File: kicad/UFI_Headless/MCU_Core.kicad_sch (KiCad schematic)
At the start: 76 parts, among them J12 FRONT, J4 SWD, J5 DBG_UART, SW1 RESET, SW2 BOOT, SW3 BTN_A, SW4 BTN_B, U11 APS6404L-3SQR-SN, U15 CSNP32GCR01-AOW, U5 STM32H723ZGT6, Y1 25MHz CL=12pF

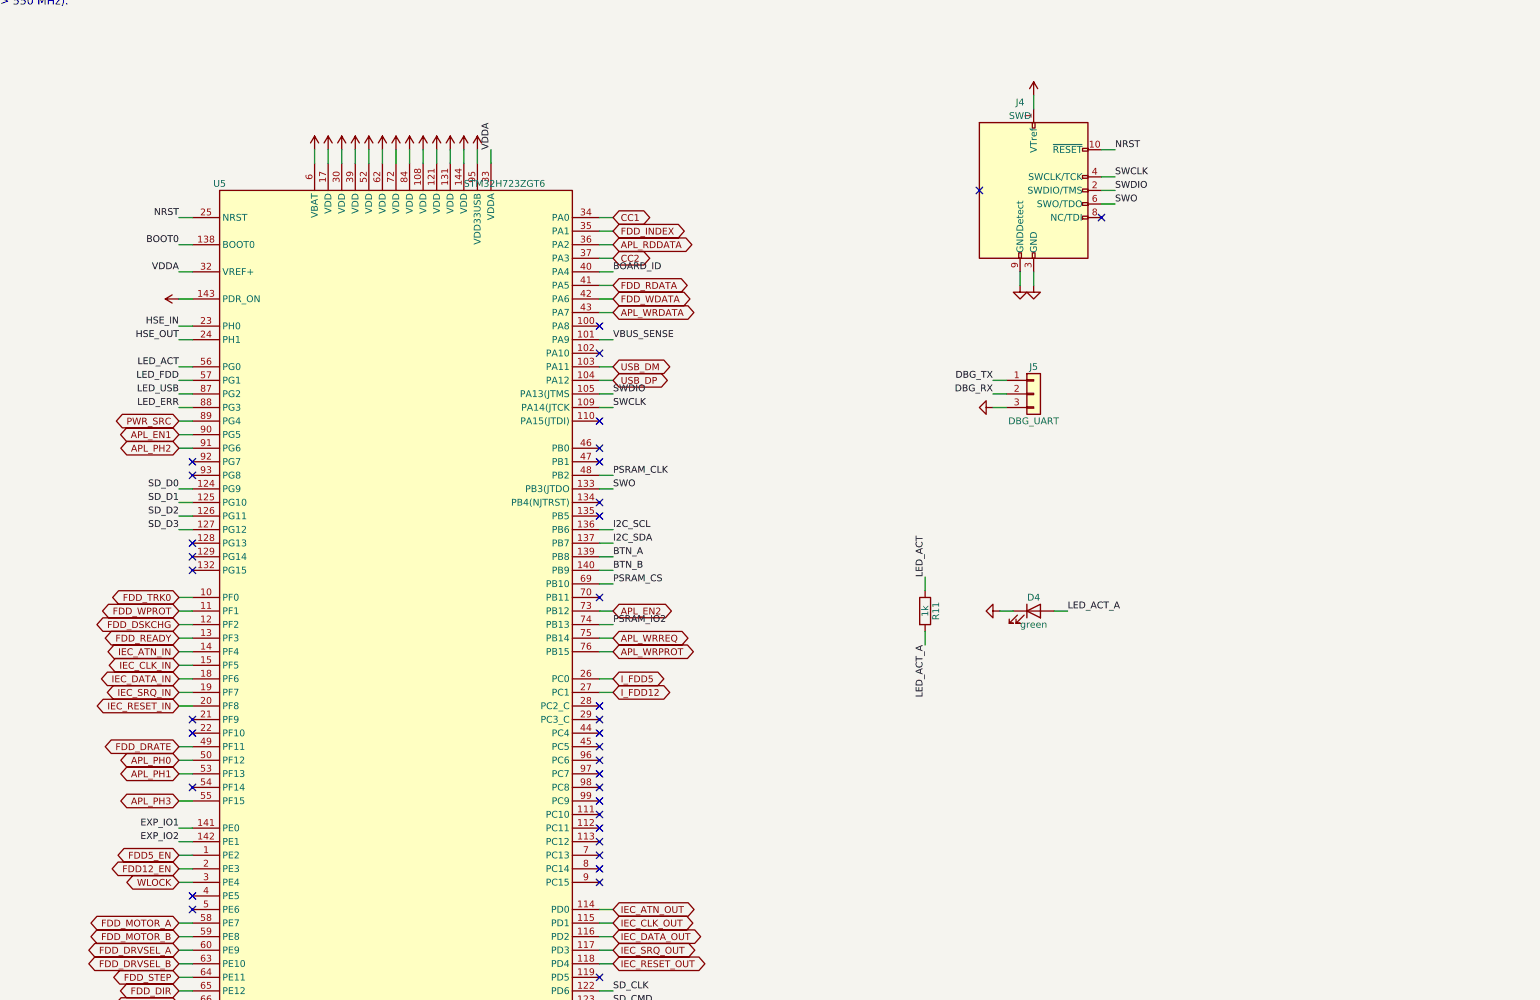
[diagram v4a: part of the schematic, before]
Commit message: KiCad v0.7 rework, schematic stage A4 with the matching firmware pin map: electronic self-test loopback, index simulation on its own timer pin, PSU-guard header, LA header - owner's constraint of 2026-10-24: the board sits in a closed enclosure, only LAN and USB stay reachable, nothing is pluggable after assembly, so no jumpers or slide switches for operation. Flux_Interface: J11 WRITE_LOCK pin header replaced by solder jumper JP4 (+3V3 to WLOCK, R33 100k pull-down and the U14 LVC1G32 hardware gate unchanged); INDEX_SIM is a global net from PE5 (TIM15_CH1, verified against the ST pin database via the embassy stm32h723zg tables) through the until now unused open-collector buffer U7F (pin 13 was tied to +5V) onto FD_INDEX, wired-OR like the J19 sync sensor, so the self-test index loop needs no wire; new loopback block U22 TS5A3166DBVR (SOT-23-5, pins 1 NO = FD_RDATA, 2 COM = FD_WDATA, 3 GND, 4 IN = LOOP_EN, 5 V+ = +5V; TI datasheet: V+ 1.65-5.5 V, VIH 2.4 V at 5 V, control input 0-5.5 V), C58 100n, R106 100k pull-down on LOOP_EN (open during reset), Q5 2N7002 pulls FD_TRK0 low with LOOP_EN; note text updated. IEC_Bus: the spare inverter U10F (input was GND, output no-connect) reads FD_WGATE back as WGATE_SENSE. MCU_Core: U5 PE5 INDEX_SIM, PG14 LOOP_EN, PG15 WGATE_SENSE, PG7 GUARD_OFF, PG8 GUARD_ERR5, PG13 GUARD_ERR12 (six no-connect flags removed); J20 GUARD 1x4 (1 GND, 2 OFF, 3 ERR5, 4 ERR12 with R107/R108 10k pull-ups) for the C64 PSU Guard board's J3; J21 LA 2x10 logic-analyser header on the 3.3 V side (1 RDATA, 3 WDATA, 5 INDEX, 7 WGATE, 9 STEP, 11 DIR, 13 SIDE, 15 DRVSEL_A, 17 MOTOR_A, 19 TRK0, 2 WPROT, 4 DSKCHG, 6 READY, 8 DENSITY, 10 INDEX_SIM, 12 LOOP_EN, 14 WGATE_SENSE, 16/18/20 GND); lib symbols TS5A3166DBVR, 2N7002, SolderJumper_2_Open, Conn_01x04, Conn_02x10_Odd_Even added to the sheets. ERC over the whole project 0 errors / 0 warnings. Firmware (same commit, as agreed): board.h/board_headless.c pin table PIN_INDEX_SIM PE5 (INDEX_SIM_AF = AF4), PIN_LOOP_EN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
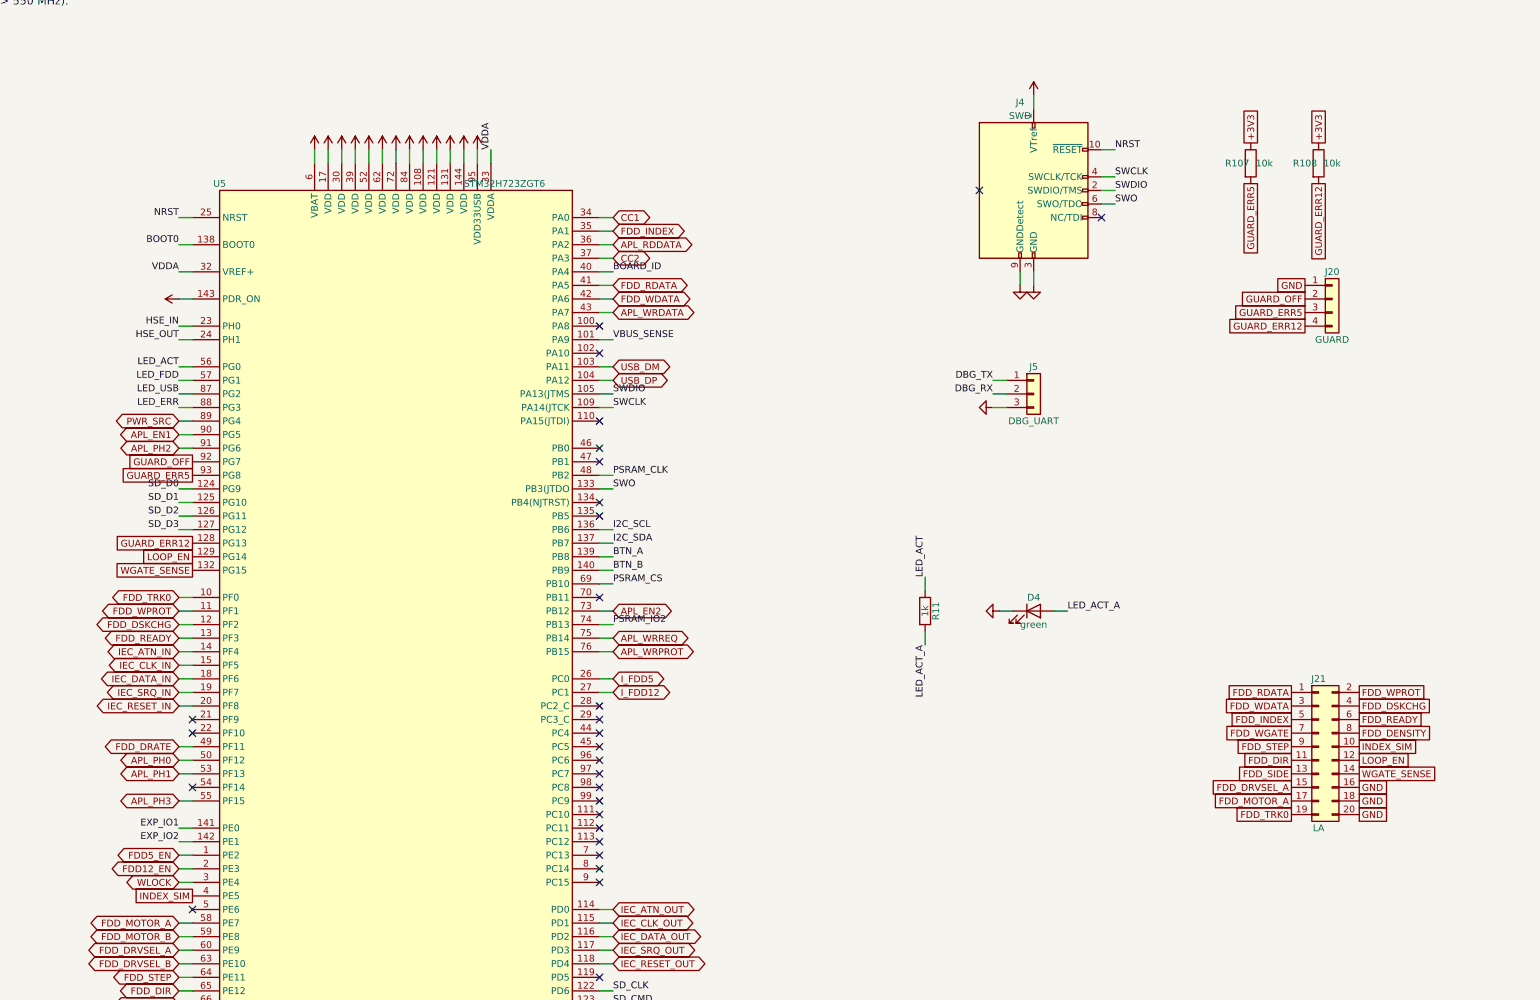
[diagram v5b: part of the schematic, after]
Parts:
- added J20: GUARD, Connector_PinHeader_2.54mm:PinHeader_1x04_P2.54mm_Vertical, symbol Connector_Generic:Conn_01x04
- added J21: LA, Connector_PinHeader_2.54mm:PinHeader_2x10_P2.54mm_Vertical, symbol Connector_Generic:Conn_02x10_Odd_Even
- added R107, R108: 10k, Resistor_SMD:R_0603_1608Metric, symbol Device:R
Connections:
- net +3V3: now also R107.1, R108.1
- net FDD_DENSITY: now also J21.8 (Pin_8)
- net FDD_DIR: now also J21.11 (Pin_11)
- net FDD_DRVSEL_A: now also J21.15 (Pin_15)
- net FDD_DSKCHG: now also J21.4 (Pin_4)
- net FDD_INDEX: now also J21.5 (Pin_5)
- net FDD_MOTOR_A: now also J21.17 (Pin_17)
- net FDD_RDATA: now also J21.1 (Pin_1)
- net FDD_READY: now also J21.6 (Pin_6)
- net FDD_SIDE: now also J21.13 (Pin_13)
- net FDD_STEP: now also J21.9 (Pin_9)
- net FDD_TRK0: now also J21.19 (Pin_19)
- net FDD_WDATA: now also J21.3 (Pin_3)
- net FDD_WGATE: now also J21.7 (Pin_7)
- net FDD_WPROT: now also J21.2 (Pin_2)
- net GND: now also J20.1 (Pin_1), J21.16 (Pin_16), J21.18 (Pin_18), J21.20 (Pin_20)
- net GUARD_ERR12: now reaches U5.128 (PG13)
- net GUARD_ERR12: now also J20.4 (Pin_4), R108.2
- net LOOP_EN: now reaches U5.129 (PG14)
- net LOOP_EN: now also J21.12 (Pin_12)
- net WGATE_SENSE: now reaches U5.132 (PG15)
- net WGATE_SENSE: now also J21.14 (Pin_14)
- net INDEX_SIM: now reaches U5.4 (PE5)
- net INDEX_SIM: now also J21.10 (Pin_10)
- net GUARD_OFF: now reaches U5.92 (PG7)
- net GUARD_OFF: now also J20.2 (Pin_2)
- net GUARD_ERR5: now reaches U5.93 (PG8)
- net GUARD_ERR5: now also J20.3 (Pin_3), R107.2
- no-connect marks 38 -> 32

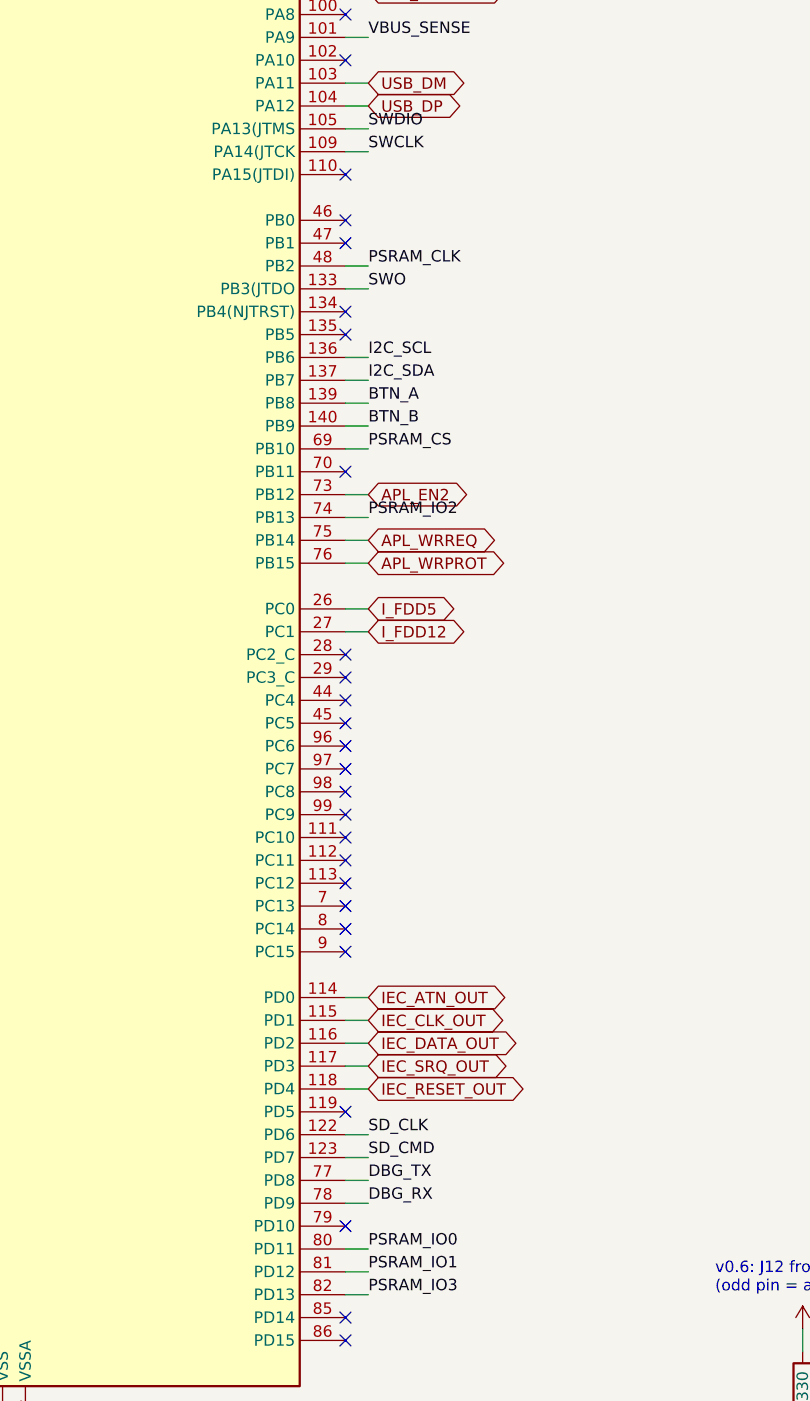
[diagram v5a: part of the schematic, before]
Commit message: KiCad v0.7 rework, schematic stage A6 with the matching firmware pin map: W5500 LAN bridge on a new sheet LAN - U23 WIZnet W5500 (LQFP-48) on SPI3 of the H723 (PC10 SCLK, PC11 MISO, PC12 MOSI, PA15 SCSn, PD5 INTn, PD10 RSTn; SPI3 pin mapping verified against the ST pin database via the embassy stm32h723zg tables, 10k pull-ups R119-R121), J22 HanRun HR911105A RJ45 with integrated 1CT:1CT magnetics, internal Bob-Smith network and LEDs (pinout from the HanRun datasheet rev. A/2 fetched from LCSC: 1 TD+, 2 TD-, 3 RD+, 4 TX centre tap, 5 RX centre tap, 6 RD-, 7 NC, 8 CHS GND to PCB ground per HanRun note, 9/10 green LED = LINK, 12/11 yellow LED = ACT via R117/R118 330 R, shield to GND); analogue front end taken from the WIZnet reference schematic W5500-Ref-ExternalMag (2015) and the W5500 datasheet v1.1.0: R112/R113 49.9 R 1% TXP/TXN to 3V3A, R114 10 R + C71 22 nF on the TX centre tap, C72/C73 6.8 nF series on RXP/RXN with R115/R116 82 R to the RX centre tap and C74 10 nF, R111 12.4k 1% on EXRES1, C61 10 nF on 1V2O, C62 4.7 uF on TOCAP, VBG left open, RSVD 23 to GND, RSVD 38-42 open (no-connect flags), PMODE0-2 through R122-R124 10k to +3V3 (all capable, auto-negotiation), Y2 25 MHz (same crystal as Y1) with C59/C60 18 pF and R109 1M, 3V3A behind FB2 600R@100MHz with C63 10 uF + C64-C68 100 nF, VDD with C69 10 uF + C70 100 nF, PWR_FLAG on 3V3A; sheet note with the sources. MCU_Core: six no-connect flags removed, global labels LAN_SCK/MISO/MOSI/CS/INT/RST on U5; root sheet LAN added as page 8. ERC over the whole project 0 errors / 0 warnings; netlist against the firmware pin table: all 61 entries match. Firmware (same commit): board.h externs PIN_LAN_SCK/MISO/MOSI/CS/INT/RST and LAN_SPI_AF = AF6, board_headless.c pin table and reset-safe init (GPIOC clock enabled, RST held low so the W5500 stays in reset until a driver exists, CS high, SPI pins and INT plain inputs); no protocol change. Docs: PLAN.md row A6 done, kicad README (LAN row in the v1.0 table, GPIO table), desig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
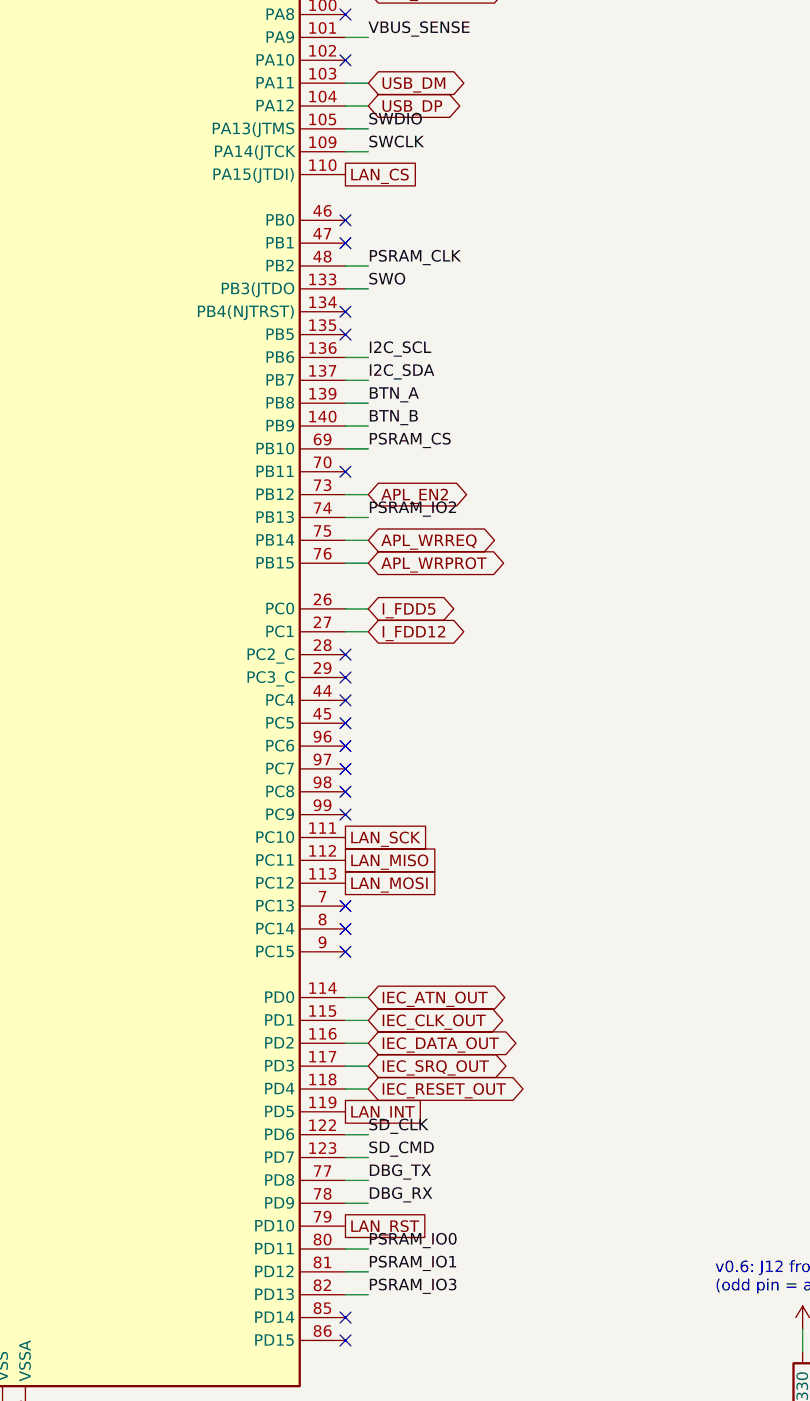
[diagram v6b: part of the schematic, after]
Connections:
- net LAN_CS: now reaches U5.110 (PA15(JTDI))
- net LAN_SCK: now reaches U5.111 (PC10)
- net LAN_MISO: now reaches U5.112 (PC11)
- net LAN_MOSI: now reaches U5.113 (PC12)
- net LAN_INT: now reaches U5.119 (PD5)
- net LAN_RST: now reaches U5.79 (PD10)
- no-connect marks 32 -> 26

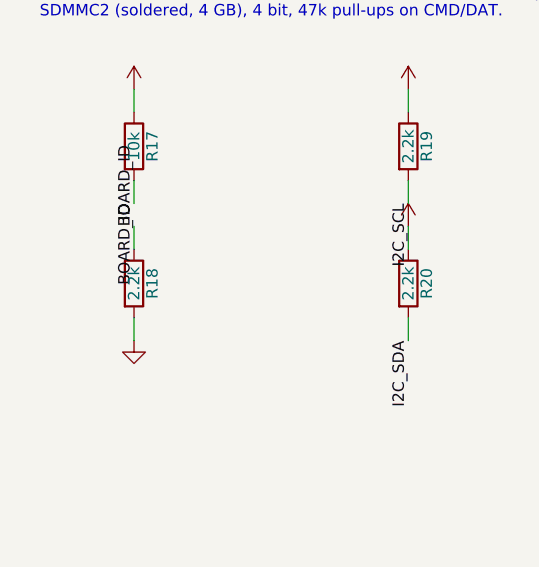
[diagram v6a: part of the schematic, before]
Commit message: KiCad v0.7 rework, stage A7: board-ID value for board v1.0 in schematic, firmware and host - MCU_Core R18 2.2k -> 22k (LCSC C31850, the same part as R9), so the BOARD_ID divider R17 10k / R18 22k gives 2269 mV, 600 mV away from the nearest existing window (v0.5 1650 mV, +-200 mV windows); board.h BOARD_ID_V10_MV 2269, ufi_v2.c ufi_board_rev() returns 10 for it, ufi_usb.c INFO text "v1.0", ufi_selftest.c board_id post knows the window, ufi_board.c ufi_board_has_apple() also true for v1.0 (the Apple port stays, caps already enable AMIGA2 for rev >= 7); ufi_firmware.h comment; protocol doc INFO row (board_rev 5/6/7 = v0.x, 10 = v1.0). Host: protocol2.board_rev_text() (5/6/7 -> v0.x, 10 -> v1.0, 0 -> unknown) used by Device2.info(), ufi info and the provenance printouts instead of the hard-coded "v0.{n}"; new test tests/test_board_rev.py. Docs: PLAN.md A7 done, kicad README (v1.0 table row, GPIO table BOARD_ID windows), function overview. ERC 0/0, ARM build 0 warnings, AXI free unchanged, gate green, ruff clean. The firmware now tells a v0.7 board (J9 index simulation, no loopback, no LAN) from a v1.0 board by the divider; feature gating on rev 10 follows with the drivers.
Claude-Session: https://claude.ai/code/session_014MdzrcyXuayppPHbfEjUrw
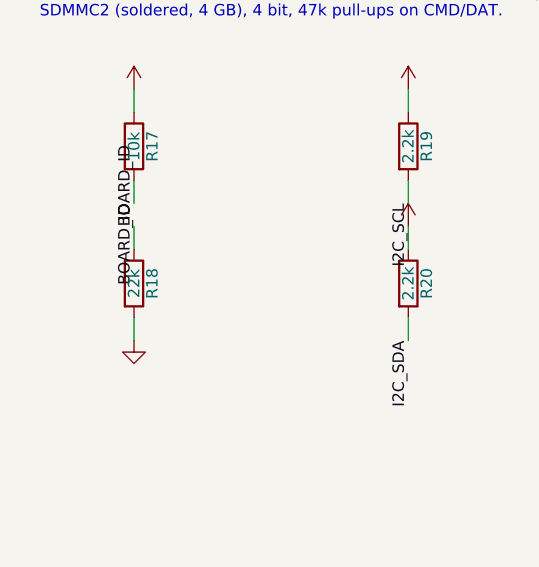
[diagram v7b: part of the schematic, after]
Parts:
- R18: value 2.2k -> 22k; LCSC C4190 -> C31850

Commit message: KiCad v0.7 rework, stage B2: board v1.0 placed and routed, DRC 0 errors / 0 warnings / 0 unconnected with schematic parity - J1 USB-C and J22 RJ45 turned so that their openings cross the input edge (rot 180 at y 2.66 / 13.11 mm; at rotation 0 both library footprints open towards the board, which is how the USB-C receptacle stood since v0.1), DRU rule idc_edge_silk extended to J1/J22/J12 (silk over the edge is clipped by the fab, justified in the file), old J9 spoke rule removed; final placement by scripts/eco/place_v10.py plus relayout_lan.py (Y2/C59/C60/R109 crystal cluster and the 3V3A filter re-laid under U23, SW3 DNP parked on B.Cu under J22 pending the owner's SW3/SW4 decision); routing: the make_pcb.sh pipeline (Freerouting 2.4.1) hit the 1800 s timeout and left 154 connections open at the 0.5-mm QFP rows of U5/U23, so the rest was done with new ECO tools - rip_net.py (corridors), fanout.py (0.5/0.25 mm dogbone vias in two rows), shrink_vias.py, batch_route.py (A* over the kicad-cli DRC JSON: every grid step checked as a segment, string-pulling per layer run, via cost in mm, start at fan-out vias, ROUTE_CLR/ROUTE_W overrides), add_vias.py (GND stitches for isolated GND pads U23.29, C29.2, U13.2/C50.2), drop_pours.py + power_pours.py (stale supply pours had bridged five missing +5V tracks at R92-R96), trim_dangling.py, hide_small_refs.py (references only for ICs, connectors, switches, crystals, fuses, inductors, D4), place_silk.py (references/texts to the nearest free silk spot, F and B); schematic: TP9-TP13 and JP4 in_bom no (set_in_bom.py), footprint Description fields synced from the symbols (netlist.py/sync_fields.py) so the parity check is clean; picture docs/layout_v1.0_2026-10-24.png; PLAN.md B2 done, kicad README layout v1.0 section, scripts/eco/README.md. Owner skill pcb-routing (installed today) applied: routing_rules.json with the 16 load nets (F1/F4 1.5 A, F2/F3 1.1 A with cut-off above 1.5 A, buck 2 A) and 24 load paths, net class Load 1.0 mm / 0.8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
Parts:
- TP10, TP11, TP12, TP13: now left out of the parts list
